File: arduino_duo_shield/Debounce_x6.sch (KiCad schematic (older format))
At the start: 25 parts

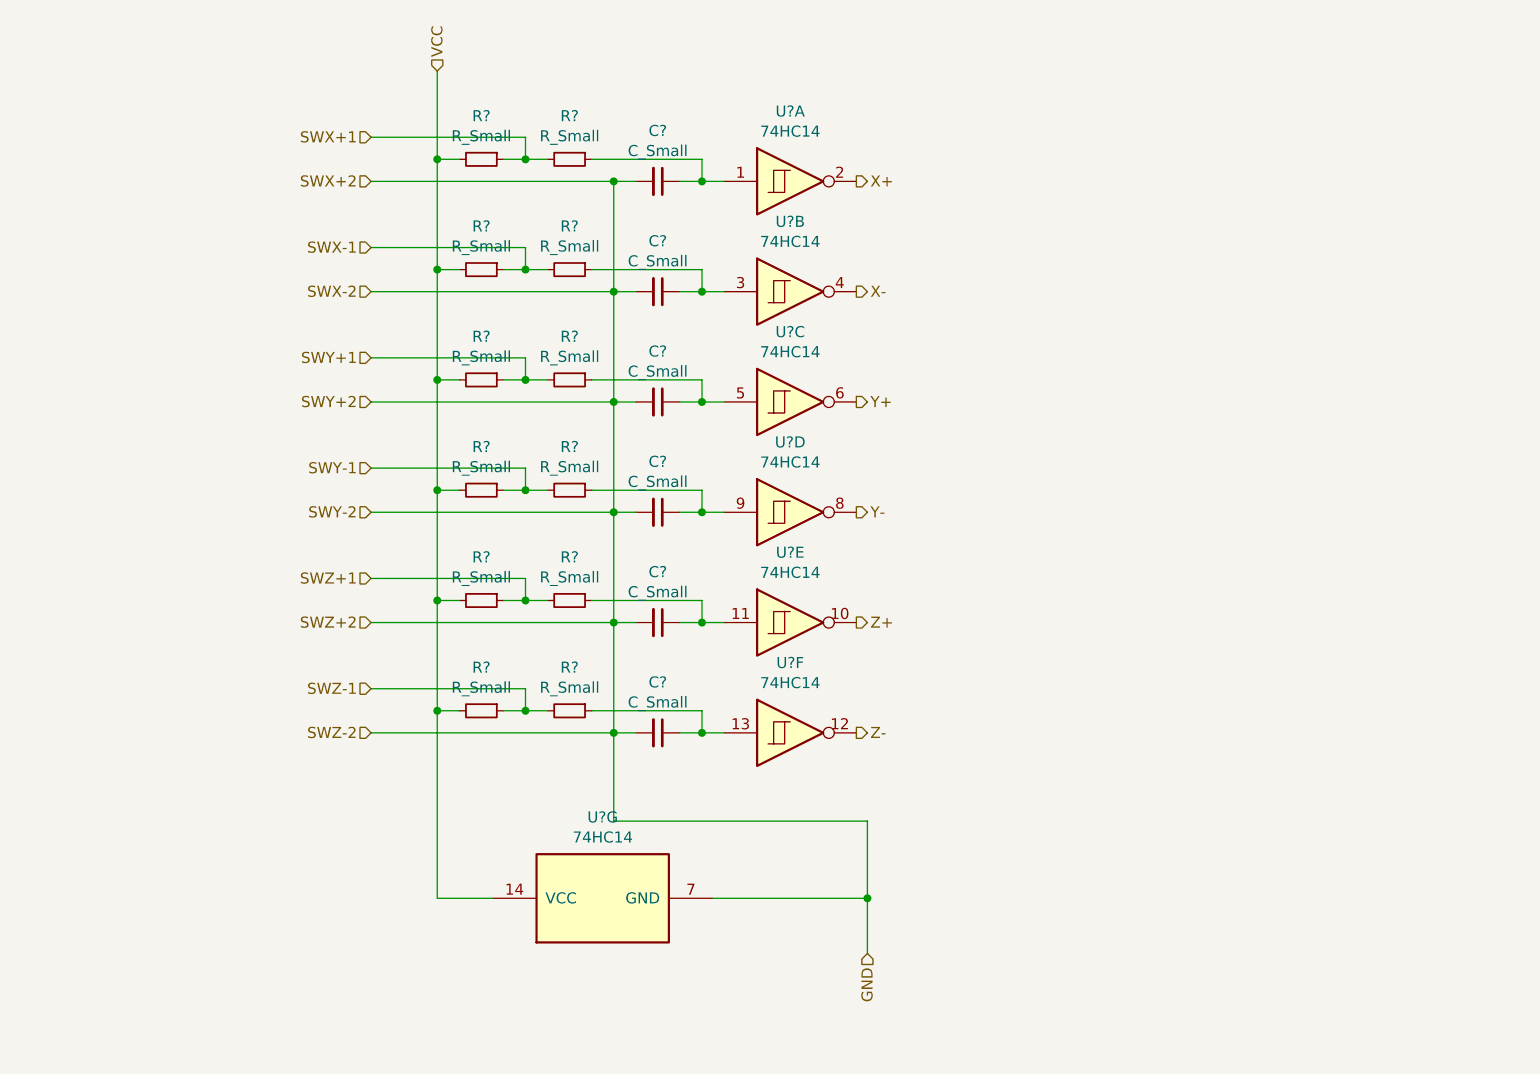
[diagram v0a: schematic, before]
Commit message: Add labels and footprints
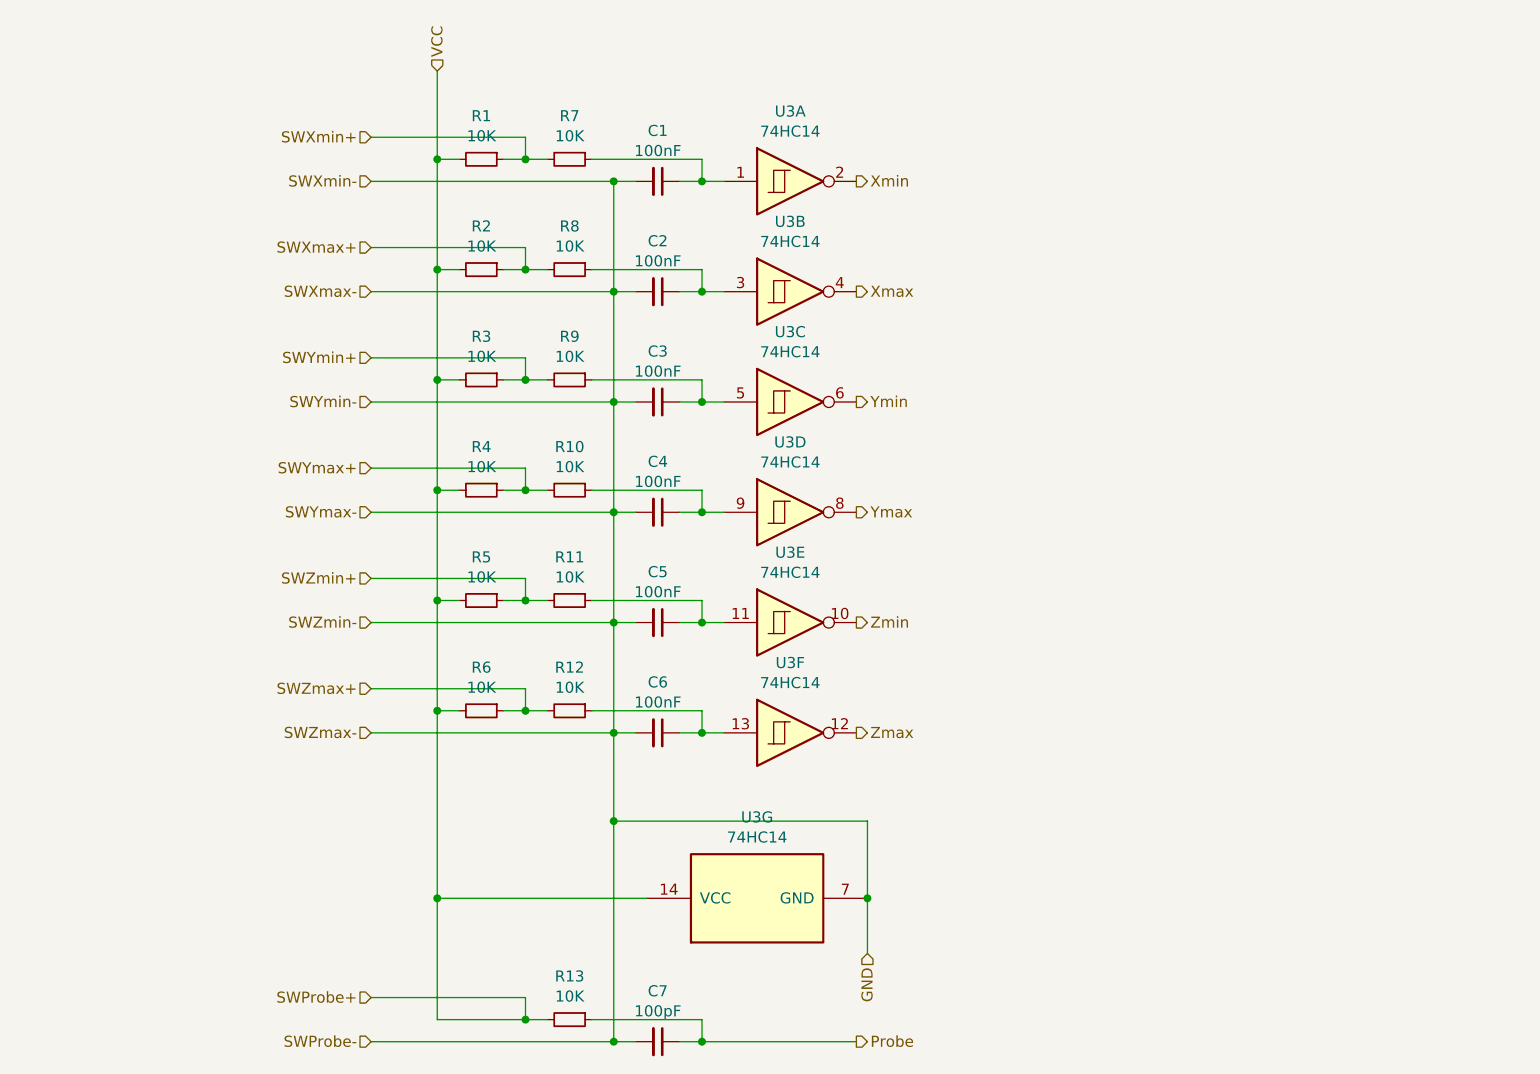
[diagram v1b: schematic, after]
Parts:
- added C7: 100pF, Capacitor_THT:C_Radial_D5.0mm_H11.0mm_P2.00mm, symbol Device:C_Small
- added R13: 10K, Resistor_THT:R_Axial_DIN0204_L3.6mm_D1.6mm_P2.54mm_Vertical, symbol Device:R_Small
- C1, C2, C3, C4, C5, C6: renamed from C?; value C_Small -> 100nF; footprint (none) -> Capacitor_THT:C_Radial_D5.0mm_H11.0mm_P2.00mm
- R1, R10, R11, R12, R2, R3, R4, R5, R6, R7, R8, R9: renamed from R?; value R_Small -> 10K; footprint (none) -> Resistor_THT:R_Axial_DIN0204_L3.6mm_D1.6mm_P2.54mm_Vertical
- U3: renamed from U?; footprint (none) -> Package_DIP:DIP-14_W7.62mm
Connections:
- net GND: now also C7.2
- net SWX+1 renamed SWXmin+
- net SWX-1 renamed SWXmax+
- net SWY+1 renamed SWYmin+
- net SWY-1 renamed SWYmax+
- net SWZ+1 renamed SWZmin+
- net SWZ-1 renamed SWZmax+
- net VCC renamed SWProbe+
- net SWProbe+: now also R13.2
- net X+ renamed Xmin
- net X- renamed Xmax
- net Y+ renamed Ymin
- net Y- renamed Ymax
- net Z+ renamed Zmin
- net Z- renamed Zmax
- new net Probe: C7.1, R13.1
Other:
- moved on the sheet: U3G

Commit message: Replace 4x 6x connectors with 1x 24x, add firmware
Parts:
- C1, C2, C3, C4, C5, C6, C7: footprint Capacitor_THT:C_Radial_D5.0mm_H11.0mm_P2.00mm -> Capacitor_THT:C_Disc_D5.0mm_W2.5mm_P2.50mm
- U3: footprint Package_DIP:DIP-14_W7.62mm -> Package_DIP:DIP-14_W7.62mm_Socket
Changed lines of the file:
@@
 F 0 "U3" H 5100 2917 50  0000 C CNN
 F 1 "74HC14" H 5100 2826 50  0000 C CNN
-F 2 "Package_DIP:DIP-14_W7.62mm" H 5100 2600 50  0001 C CNN
+F 2 "Package_DIP:DIP-14_W7.62mm_Socket" H 5100 2600 50  0001 C CNN
 F 3 "http://www.ti.com/lit/gpn/sn74HC14" H 5100 2600 50  0001 C CNN
 	1    5100 2600
@@
 F 0 "C1" V 4271 2600 50  0000 C CNN
 F 1 "100nF" V 4362 2600 50  0000 C CNN
-F 2 "Capacitor_THT:C_Radial_D5.0mm_H11.0mm_P2.00mm" H 4500 2600 50  0001 C CNN
+F 2 "Capacitor_THT:C_Disc_D5.0mm_W2.5mm_P2.50mm" H 4500 2600 50  0001 C CNN
 F 3 "~" H 4500 2600 50  0001 C CNN
 	1    4500 2600
@@
 F 0 "U3" H 5100 3417 50  0000 C CNN
 F 1 "74HC14" H 5100 3326 50  0000 C CNN
-F 2 "Package_DIP:DIP-14_W7.62mm" H 5100 3100 50  0001 C CNN
+F 2 "Package_DIP:DIP-14_W7.62mm_Socket" H 5100 3100 50  0001 C CNN
 F 3 "http://www.ti.com/lit/gpn/sn74HC14" H 5100 3100 50  0001 C CNN
 	2    5100 3100
@@
 F 0 "U3" H 5100 3917 50  0000 C CNN
 F 1 "74HC14" H 5100 3826 50  0000 C CNN
-F 2 "Package_DIP:DIP-14_W7.62mm" H 5100 3600 50  0001 C CNN
+F 2 "Package_DIP:DIP-14_W7.62mm_Socket" H 5100 3600 50  0001 C CNN
 F 3 "http://www.ti.com/lit/gpn/sn74HC14" H 5100 3600 50  0001 C CNN
 	3    5100 3600
@@
 F 0 "U3" H 5100 4417 50  0000 C CNN
 F 1 "74HC14" H 5100 4326 50  0000 C CNN
-F 2 "Package_DIP:DIP-14_W7.62mm" H 5100 4100 50  0001 C CNN
+F 2 "Package_DIP:DIP-14_W7.62mm_Socket" H 5100 4100 50  0001 C CNN
 F 3 "http://www.ti.com/lit/gpn/sn74HC14" H 5100 4100 50  0001 C CNN
 	4    5100 4100
@@
 F 0 "U3" H 5100 4917 50  0000 C CNN
 F 1 "74HC14" H 5100 4826 50  0000 C CNN
-F 2 "Package_DIP:DIP-14_W7.62mm" H 5100 4600 50  0001 C CNN
+F 2 "Package_DIP:DIP-14_W7.62mm_Socket" H 5100 4600 50  0001 C CNN
 F 3 "http://www.ti.com/lit/gpn/sn74HC14" H 5100 4600 50  0001 C CNN
 	5    5100 4600
@@
 F 0 "U3" V 5317 5850 50  0000 C CNN
 F 1 "74HC14" V 5226 5850 50  0000 C CNN
-F 2 "Package_DIP:DIP-14_W7.62mm" H 4950 5850 50  0001 C CNN
+F 2 "Package_DIP:DIP-14_W7.62mm_Socket" H 4950 5850 50  0001 C CNN
 F 3 "http://www.ti.com/lit/gpn/sn74HC14" H 4950 5850 50  0001 C CNN
 	7    4950 5850
@@
 F 0 "U3" H 5100 5417 50  0000 C CNN
 F 1 "74HC14" H 5100 5326 50  0000 C CNN
-F 2 "Package_DIP:DIP-14_W7.62mm" H 5100 5100 50  0001 C CNN
+F 2 "Package_DIP:DIP-14_W7.62mm_Socket" H 5100 5100 50  0001 C CNN
 F 3 "http://www.ti.com/lit/gpn/sn74HC14" H 5100 5100 50  0001 C CNN
 	6    5100 5100
@@
 F 0 "C2" V 4271 3100 50  0000 C CNN
 F 1 "100nF" V 4362 3100 50  0000 C CNN
-F 2 "Capacitor_THT:C_Radial_D5.0mm_H11.0mm_P2.00mm" H 4500 3100 50  0001 C CNN
+F 2 "Capacitor_THT:C_Disc_D5.0mm_W2.5mm_P2.50mm" H 4500 3100 50  0001 C CNN
 F 3 "~" H 4500 3100 50  0001 C CNN
 	1    4500 3100
@@
 F 0 "C3" V 4271 3600 50  0000 C CNN
 F 1 "100nF" V 4362 3600 50  0000 C CNN
-F 2 "Capacitor_THT:C_Radial_D5.0mm_H11.0mm_P2.00mm" H 4500 3600 50  0001 C CNN
+F 2 "Capacitor_THT:C_Disc_D5.0mm_W2.5mm_P2.50mm" H 4500 3600 50  0001 C CNN
 F 3 "~" H 4500 3600 50  0001 C CNN
 	1    4500 3600
@@
 F 0 "C4" V 4271 4100 50  0000 C CNN
 F 1 "100nF" V 4362 4100 50  0000 C CNN
-F 2 "Capacitor_THT:C_Radial_D5.0mm_H11.0mm_P2.00mm" H 4500 4100 50  0001 C CNN
+F 2 "Capacitor_THT:C_Disc_D5.0mm_W2.5mm_P2.50mm" H 4500 4100 50  0001 C CNN
 F 3 "~" H 4500 4100 50  0001 C CNN
 	1    4500 4100
@@
 F 0 "C5" V 4271 4600 50  0000 C CNN
 F 1 "100nF" V 4362 4600 50  0000 C CNN
-F 2 "Capacitor_THT:C_Radial_D5.0mm_H11.0mm_P2.00mm" H 4500 4600 50  0001 C CNN
+F 2 "Capacitor_THT:C_Disc_D5.0mm_W2.5mm_P2.50mm" H 4500 4600 50  0001 C CNN
 F 3 "~" H 4500 4600 50  0001 C CNN
 	1    4500 4600
@@
 F 0 "C6" V 4271 5100 50  0000 C CNN
 F 1 "100nF" V 4362 5100 50  0000 C CNN
-F 2 "Capacitor_THT:C_Radial_D5.0mm_H11.0mm_P2.00mm" H 4500 5100 50  0001 C CNN
+F 2 "Capacitor_THT:C_Disc_D5.0mm_W2.5mm_P2.50mm" H 4500 5100 50  0001 C CNN
 F 3 "~" H 4500 5100 50  0001 C CNN
 	1    4500 5100
@@
 F 0 "C7" V 4271 6500 50  0000 C CNN
 F 1 "100pF" V 4362 6500 50  0000 C CNN
-F 2 "Capacitor_THT:C_Radial_D5.0mm_H11.0mm_P2.00mm" H 4500 6500 50  0001 C CNN
+F 2 "Capacitor_THT:C_Disc_D5.0mm_W2.5mm_P2.50mm" H 4500 6500 50  0001 C CNN
 F 3 "~" H 4500 6500 50  0001 C CNN
 	1    4500 6500

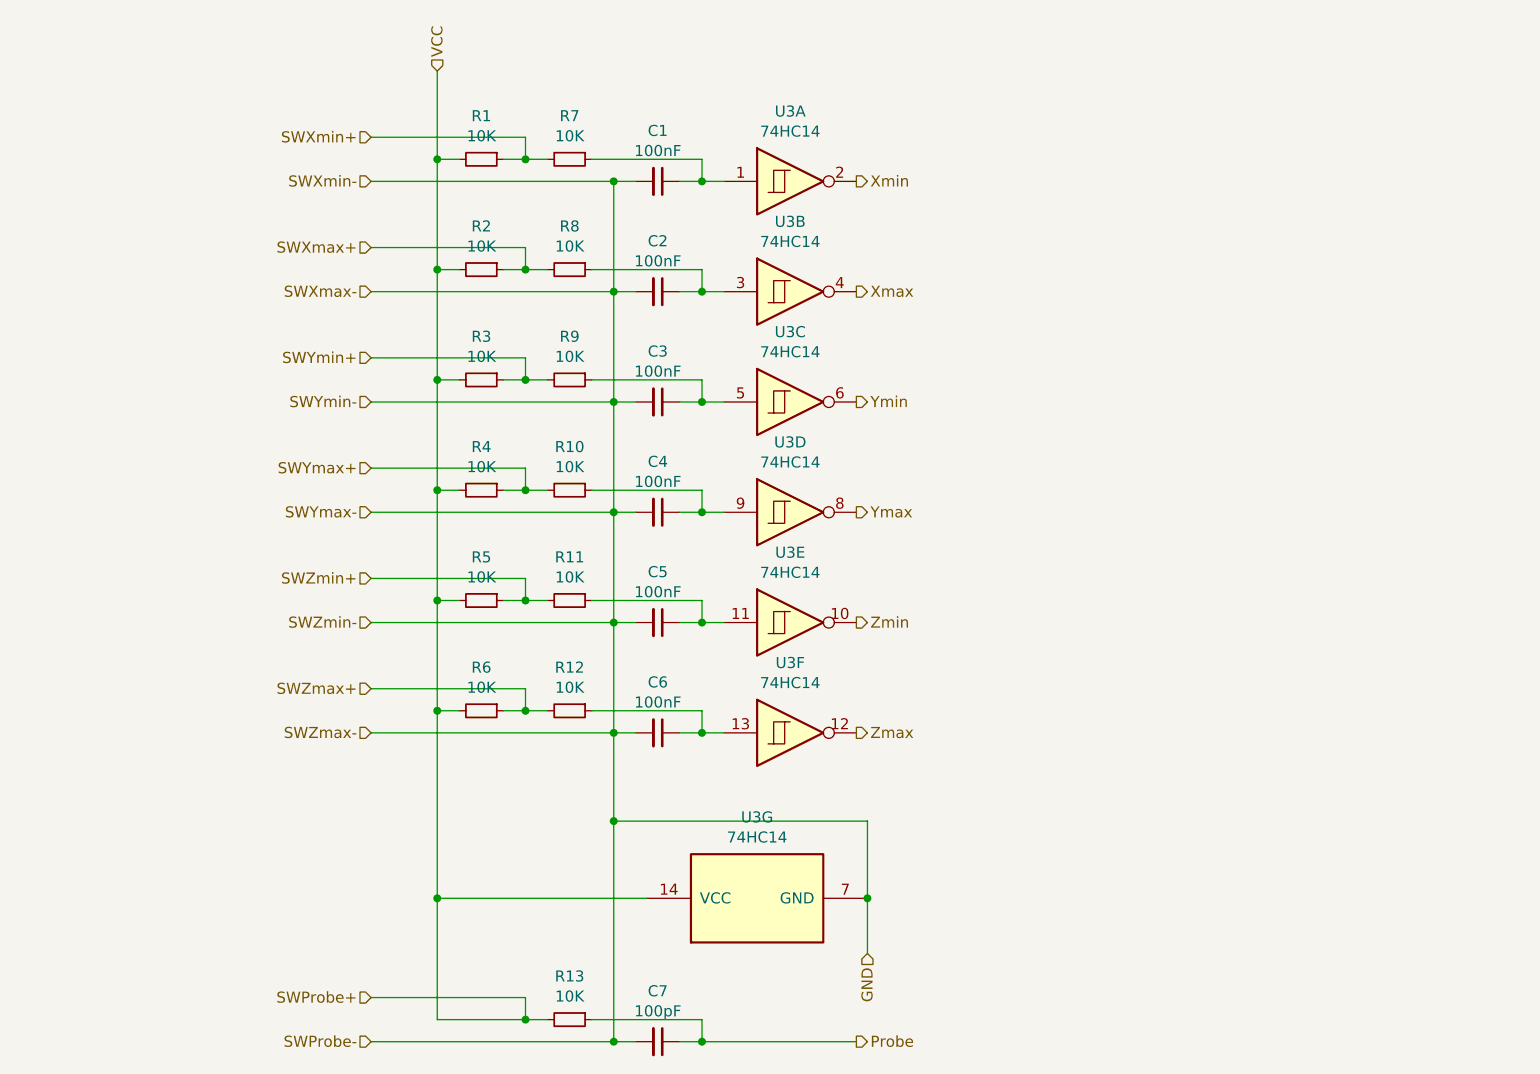
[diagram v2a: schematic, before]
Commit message: Use only 1 VPOW in spindle control
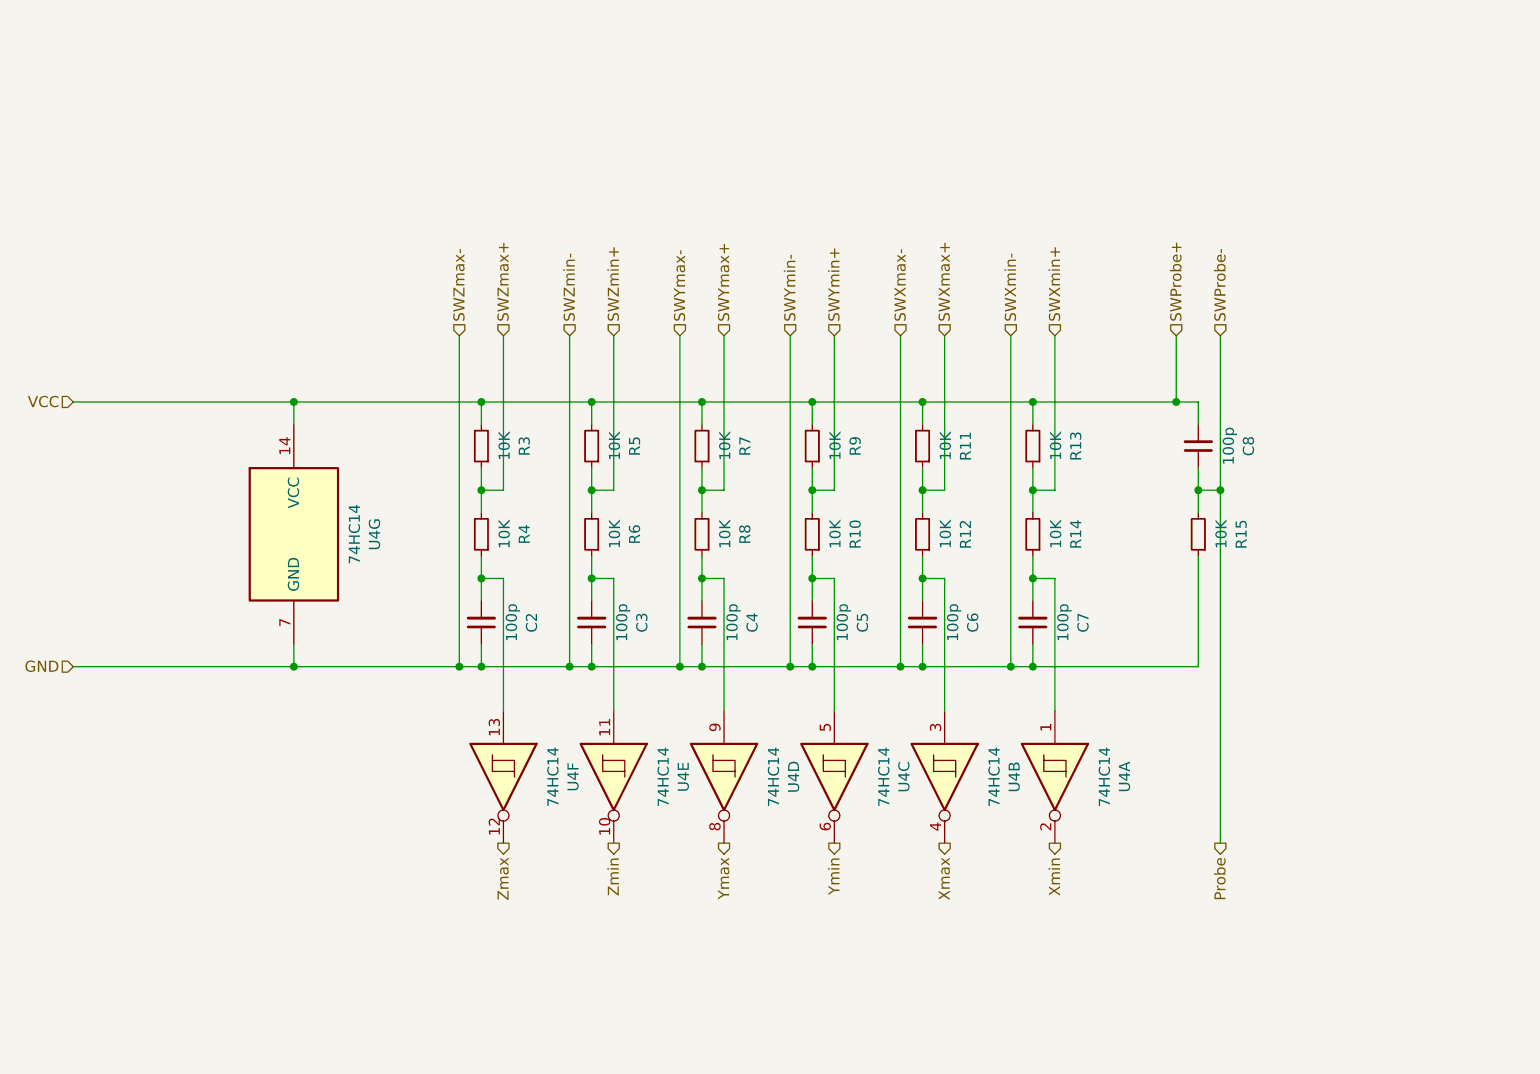
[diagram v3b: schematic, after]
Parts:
- C1, C2, C3, C4, C5, C6: value 100nF -> 100p
- C7: value 100pF -> 100p
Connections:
- net GND: now also C1.1, C2.1, C3.1, C4.1, C5.1, C6.1, R13.1; no longer C1.2, C2.2, C3.2, C4.2, C5.2, C6.2, C7.2
- net Probe: now also R13.2; no longer R13.1
- net SWProbe+: now also C7.2; no longer R13.2
- net at R7.1, U3.1: now also C1.2; no longer C1.1
- net at R8.1, U3.3: now also C2.2; no longer C2.1
- net at R9.1, U3.5: now also C3.2; no longer C3.1
- net at R10.1, U3.9: now also C4.2; no longer C4.1
- net at R11.1, U3.11: now also C5.2; no longer C5.1
- net at R12.1, U3.13: now also C6.2; no longer C6.1
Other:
- moved on the sheet: C2, C3, C4, C5, C6, C7, C8, R10, R11, R12, R13, R14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

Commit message: Complete wiring
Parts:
- removed C7: 100p, Capacitor_THT:C_Disc_D5.0mm_W2.5mm_P2.50mm, symbol Device:C_Small
- removed R13: 10K, Resistor_THT:R_Axial_DIN0204_L3.6mm_D1.6mm_P2.54mm_Vertical, symbol Device:R_Small
- added C9: 100p, Capacitor_THT:C_Disc_D3.0mm_W2.0mm_P2.50mm, symbol Device:C_Small
- added R19, R20: 10K, Resistor_THT:R_Axial_DIN0204_L3.6mm_D1.6mm_P5.08mm_Horizontal, symbol Device:R_Small
- added U6: 74HC14, Package_DIP:DIP-14_W7.62mm_Socket, symbol 74xx:74HC14
- C1, C2, C3, C4, C5, C6: footprint Capacitor_THT:C_Disc_D5.0mm_W2.5mm_P2.50mm -> Capacitor_THT:C_Disc_D3.0mm_W2.0mm_P2.50mm
- R1, R10, R11, R12, R2, R3, R4, R5, R6, R7, R8, R9: footprint Resistor_THT:R_Axial_DIN0204_L3.6mm_D1.6mm_P2.54mm_Vertical -> Resistor_THT:R_Axial_DIN0204_L3.6mm_D1.6mm_P5.08mm_Horizontal
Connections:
- net GND: now also C9.1, U6.7 (GND)
- net Probe: now also U6.2
- net SWProbe+: now also R19.1, R20.2; no longer R1.2, R2.2, R3.2, R4.2, R5.2, R6.2, U3.14 (VCC)
- net Xmax: now also U3.10; no longer U3.4
- net Xmin: now also U3.12; no longer U3.2
- net Ymax: now also U3.2; no longer U3.8
- net Ymin: now also U3.8; no longer U3.6
- net Zmax: now also U3.6; no longer U3.12
- net Zmin: now also U3.4; no longer U3.10
- net at C1.2, R7.1: now also U3.13; no longer U3.1
- net at C2.2, R8.1: now also U3.11; no longer U3.3
- net at C3.2, R9.1: now also U3.9; no longer U3.5
- net at C4.2, R10.1: now also U3.1; no longer U3.9
- net at C5.2, R11.1: now also U3.3; no longer U3.11
- net at C6.2, R12.1: now also U3.5; no longer U3.13
- new net: C9.2, R20.1, U6.1
- new net VCC: R1.2, R19.2, R2.2, R3.2, R4.2, R5.2, R6.2, U3.14 (VCC), U6.14 (VCC)
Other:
- moved on the sheet: C2, C3, C4, C5, C6, C7, R10, R11, R12, R13, R14, R3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
